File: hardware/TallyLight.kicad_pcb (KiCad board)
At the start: 4 copper layers, 68 x 68 mm, 136 parts, among them J1 Hanrun HY931147C, J2 USB_C_Receptacle_USB2.0, J3 Strapping, J4 UART, SW1 SW_Push, T2 HR051067, U1 ESP32-C3-MINI-1, U10 EL357N(B)(TA)-G, U11 CJ431, U2 KSZ8851SNL, U3 SRV05-4, U5 AMS1117-3.3, U7 SRV05-4, U9 Si3402-B, Y1 25MHz

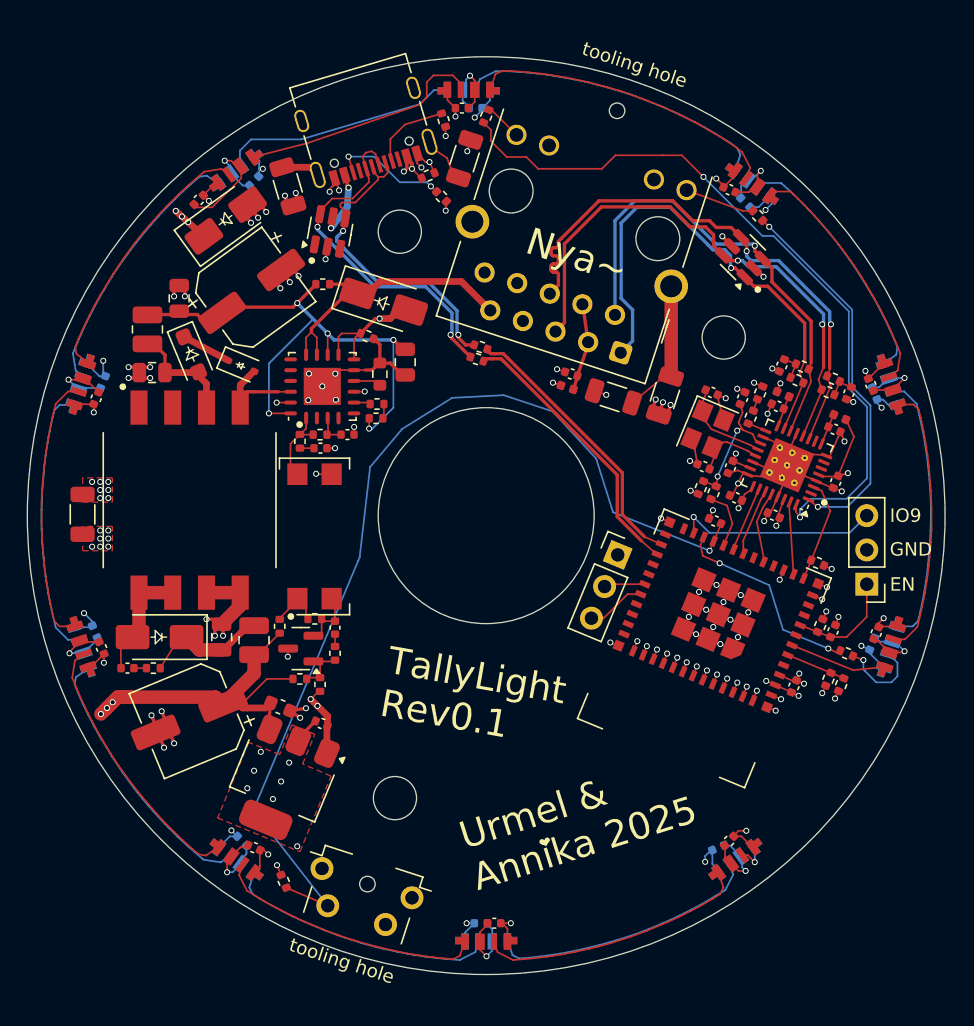
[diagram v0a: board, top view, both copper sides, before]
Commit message: hardware: replace ESP32-C3 MINI by more common WROOM-02 module
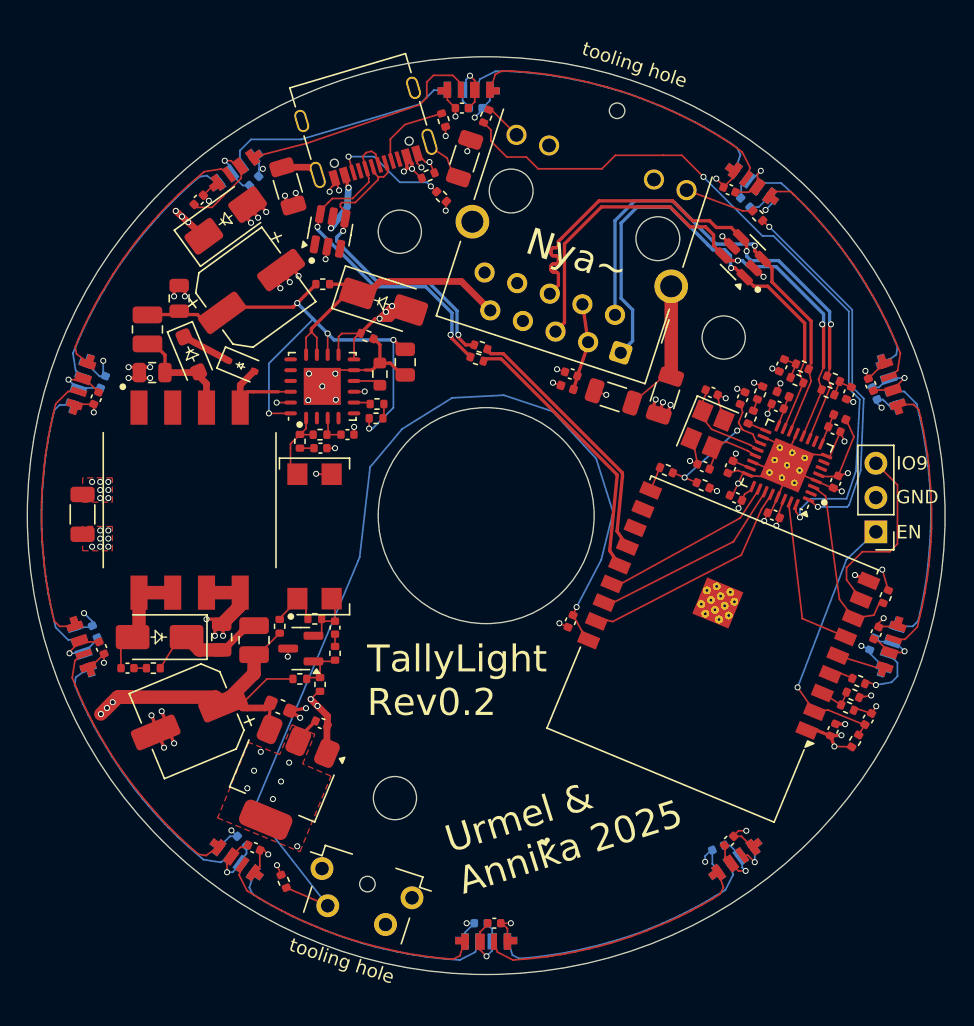
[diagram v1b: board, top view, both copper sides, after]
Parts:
- removed J4: UART, Connector_PinHeader_2.54mm:PinHeader_1x03_P2.54mm_Vertical
- removed U1: ESP32-C3-MINI-1, ESP32_C3:ESP32-C3-MINI-1
- added U4: ESP32-C3-WROOM-02, RF_Module:ESP32-C3-WROOM-02, F.Cu at (168.0, 107.0)
- moved C14 13.0 mm to (156.2, 107.8), turned to -112.5 degrees
- moved R2 8.93 mm to (177.3, 116.7), turned to 59.5 degrees
- moved C1 7.02 mm to (178.3, 115.1), turned to -120.5 degrees
- moved R4 5.63 mm to (179.6, 106.0), turned to 67.5 degrees
- moved C2 4.34 mm to (175.7, 115.9), turned to 67.5 degrees
- moved J3 3.94 mm to (178.9, 101.2)
- moved R3 3.88 mm to (163.3, 96.6), turned to 157.5 degrees
- moved R1 2.24 mm to (177.6, 112.3)
- moved R50 2.16 mm to (177.2, 113.3), turned to 157.5 degrees
- moved R49 1.77 mm to (176.8, 114.2), turned to -22.5 degrees
- moved R5 0.24 mm to (166.1, 97.8), turned to -22.5 degrees
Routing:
- net GND: track 182.8 -> 143.7 mm, vias 103 -> 70
- net /Logic/LED_Din: track 14.9 -> 1.11 mm, vias 2 -> 0
- net /Logic/EN: track 8.14 -> 20.2 mm, vias 0 -> 1
- net Net-(U2-SCLK): track 5.21 -> 16.5 mm
- net Net-(U2-SO): track 4.82 -> 14.3 mm
- net Net-(U2-~{CS}): track 4.69 -> 13.2 mm
- net Net-(U2-SI): track 5.10 -> 12.2 mm
- net Net-(U2-~{INT}): track 7.66 -> 13.2 mm
- net Net-(J4-Pin_3): track 4.48 -> 0.00 mm
- net /Logic/PoE-: track 18.3 -> 22.6 mm, vias 1 -> 3
- net /LEDs top/Din: track 7.27 -> 3.50 mm
- net Net-(J4-Pin_2): track 3.04 -> 0.00 mm
- net +3V3: track 13.5 -> 16.2 mm, vias 19 -> 18
- net Net-(U4-IO10): track 4.42 -> 1.86 mm
- net /LEDs bottom/Dout: track 6.48 -> 4.61 mm
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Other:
- board text added: "TallyLight Rev0.2"
- board text removed: "TallyLight Rev0.1"

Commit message: hardware: add testpoints to flyback converter and SPI MAC + Phy
Add testpoints to all critical section that might require in-circuit
debugging
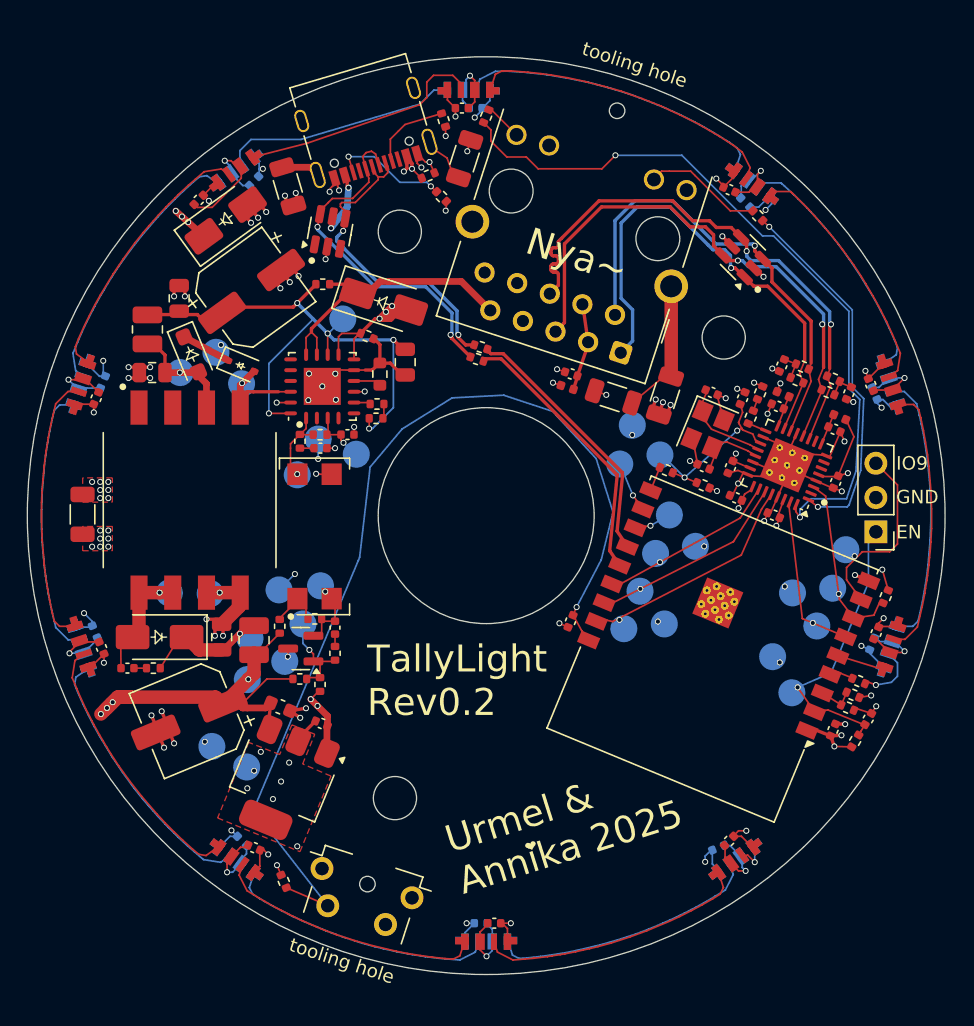
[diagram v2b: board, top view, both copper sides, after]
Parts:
- added TP1: EROUT, TestPoint_no_outline:TestPoint_Pad_D2.0mm_no_outline, B.Cu at (136.0, 97.0)
- added TP10: VOPTO, TestPoint_no_outline:TestPoint_Pad_D2.0mm_no_outline, B.Cu at (137.7, 105.2)
- added TP11: GND, TestPoint:TestPoint_Pad_D2.0mm, B.Cu at (134.7, 105.5)
- added TP12: VOUT, TestPoint_no_outline:TestPoint_Pad_D2.0mm_no_outline, B.Cu at (132.5, 109.1)
- added TP13: VOUT_FLYBACK, TestPoint_no_outline:TestPoint_Pad_D2.0mm_no_outline, B.Cu at (126.5, 105.7)
- added TP14: GND2, TestPoint_polygon_outline:TestPoint_Pad_D2.0mm_trianglular_outline, B.Cu at (130.0, 87.9)
- added TP15: RXD, TestPoint_no_outline:TestPoint_Pad_D2.0mm_no_outline, B.Cu at (159.9, 96.2)
- added TP16: TXD, TestPoint_no_outline:TestPoint_Pad_D2.0mm_no_outline, B.Cu at (163.6, 100.0)
- added TP17: SI, TestPoint_no_outline:TestPoint_Pad_D2.0mm_no_outline, B.Cu at (174.5, 108.2)
- added TP18: ~{INT}, TestPoint_no_outline:TestPoint_Pad_D2.0mm_no_outline, B.Cu at (175.7, 105.4)
- added TP19: ~{RST}, TestPoint_no_outline:TestPoint_Pad_D2.0mm_no_outline, B.Cu at (162.9, 95.5)
- added TP2: GND2, TestPoint_polygon_outline:TestPoint_Pad_D2.0mm_trianglular_outline, B.Cu at (137.6, 94.3)
- added TP20: SCLK, TestPoint_no_outline:TestPoint_Pad_D2.0mm_no_outline, B.Cu at (160.2, 108.4)
- added TP21: SO, TestPoint_no_outline:TestPoint_Pad_D2.0mm_no_outline, B.Cu at (161.4, 105.6)
- added TP22: ~{CS}, TestPoint_no_outline:TestPoint_Pad_D2.0mm_no_outline, B.Cu at (162.6, 102.8)
- added TP23: GND, TestPoint:TestPoint_Pad_D2.0mm, B.Cu at (129.6, 105.8)
- added TP24: EN, TestPoint_no_outline:TestPoint_Pad_D2.0mm_no_outline, B.Cu at (172.7, 113.1)
- added TP25: GND, TestPoint:TestPoint_Pad_D2.0mm, B.Cu at (171.2, 110.5)
- added TP26: IO9, TestPoint_no_outline:TestPoint_Pad_D2.0mm_no_outline, B.Cu at (176.7, 102.5)
- added TP27: GND, TestPoint:TestPoint_Pad_D2.0mm, B.Cu at (165.5, 102.3)
- added TP28: GND, TestPoint:TestPoint_Pad_D2.0mm, B.Cu at (163.2, 108.0)
- added TP29: GND, TestPoint:TestPoint_Pad_D2.0mm, B.Cu at (172.7, 105.7)
- added TP3: VOUT_FLT, TestPoint_no_outline:TestPoint_Pad_D2.0mm_no_outline, B.Cu at (132.3, 112.2)
- added TP30: GND, TestPoint:TestPoint_Pad_D2.0mm, B.Cu at (160.8, 93.3)
- added TP31: +3v3, TestPoint_no_outline:TestPoint_Pad_D2.0mm_no_outline, B.Cu at (132.2, 118.6)
- added TP32: GND, TestPoint:TestPoint_Pad_D2.0mm, B.Cu at (129.7, 117.1)
- added TP4: GND, TestPoint:TestPoint_Pad_D2.0mm, B.Cu at (135.1, 110.8)
- added TP5: VCC_FLYBACK, TestPoint_no_outline:TestPoint_Pad_D2.0mm_no_outline, B.Cu at (127.3, 89.4)
- added TP6: VCC_PoE, TestPoint_no_outline:TestPoint_Pad_D2.0mm_no_outline, B.Cu at (139.4, 85.4)
- added TP7: SW_FLYBACK, TestPoint_no_outline:TestPoint_Pad_D2.0mm_no_outline, B.Cu at (131.9, 90.2)
- added TP8: VCC_AUX, TestPoint_no_outline:TestPoint_Pad_D2.0mm_no_outline, B.Cu at (140.4, 95.5)
- added TP9: VREF, TestPoint_no_outline:TestPoint_Pad_D2.0mm_no_outline, B.Cu at (136.4, 108.0)
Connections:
- J1 pad 11: Net-(J1-Pad11) -> +3V3
- J1 pad 12: GND -> Net-(J1-Pad12)
- R36 pad 2: Net-(J1-Pad11) -> Net-(J1-Pad12)
- U4 pad 11: unconnected-(U4-IO20/RXD-Pad11) -> Net-(U4-IO20/RXD)
- U4 pad 12: unconnected-(U4-IO21/TXD-Pad12) -> Net-(U4-IO21/TXD)
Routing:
- net Net-(J1-Pad12): track 0.00 -> 8.83 mm
- net Net-(J1-Pad11): track 5.19 -> 0.00 mm
- net Net-(U4-IO20/RXD): track 0.00 -> 3.74 mm, vias 0 -> 1
- net Net-(U11-REF): track 3.99 -> 7.07 mm, vias 0 -> 1
- net Net-(U4-IO21/TXD): track 0.00 -> 2.74 mm, vias 0 -> 1
- net Net-(U2-~{RST}): track 11.3 -> 13.9 mm
- net Net-(U9-VDD): track 2.23 -> 4.21 mm, vias 0 -> 1
- net GND: track 143.7 -> 145.3 mm, vias 70 -> 78
- net Net-(U9-FB): track 43.0 -> 44.5 mm
- net GND2: track 12.7 -> 14.2 mm, vias 21 -> 23
- net /Logic/EN: track 20.2 -> 21.0 mm
- net /Logic/IO9: track 13.9 -> 14.0 mm, vias 0 -> 1
- net Net-(U2-SCLK): track 16.5 -> 16.7 mm, vias 0 -> 1
- net Net-(U2-SI): vias 0 -> 1
- net Net-(U2-~{CS}): vias 0 -> 1
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
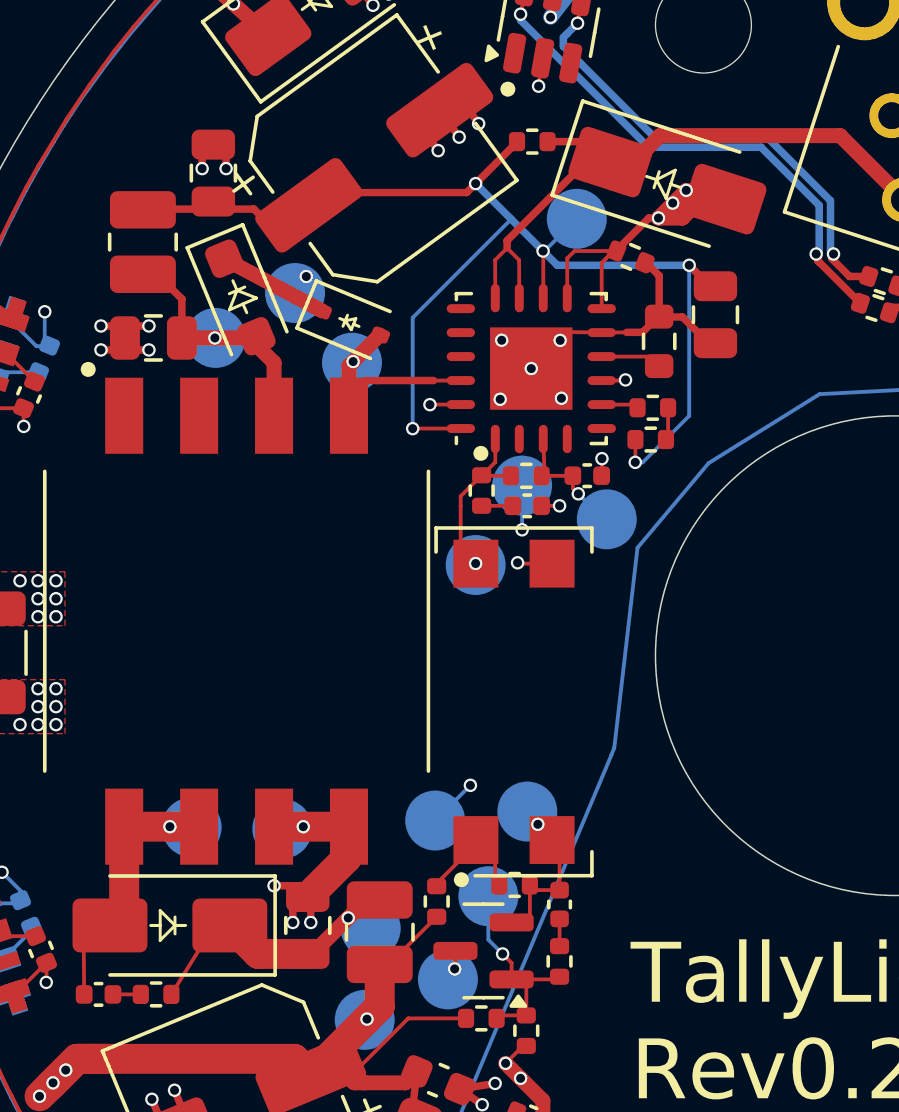
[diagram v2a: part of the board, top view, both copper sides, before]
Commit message: hardware: add small thermal plane to PoE controller
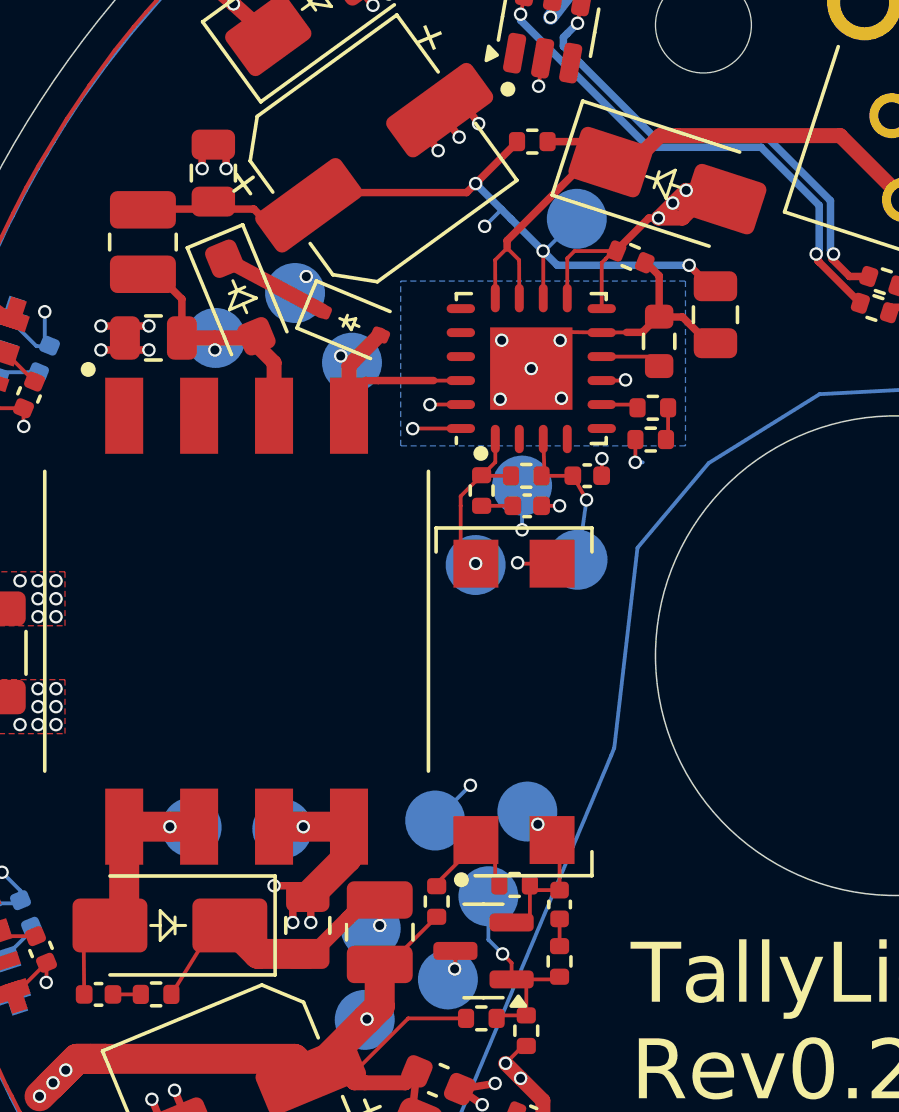
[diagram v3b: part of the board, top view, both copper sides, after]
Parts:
- moved TP8 1.67 mm to (139.4, 96.8)
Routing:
- net Net-(D28-K): track 11.7 -> 12.6 mm
- net Net-(U9-FB): track 44.5 -> 44.8 mm, vias 5 -> 6
- added copper zone on B.Cu, net Net-(C49-Pad2)
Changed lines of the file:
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@@
 	(footprint "TestPoint_no_outline:TestPoint_Pad_D2.0mm_no_outline"
 		(layer "B.Cu")
-		(at 140.375 95.45 180)
+		(at 139.4 96.8 180)
 		(descr "SMD pad as test Point, diameter 2.0mm")
 		(tags "test point SMD pad")
@@
 		(net 3)
 	)
+	(segment
+		(start 127.3 89.4)
+		(end 127.3 89.8)
+		(width 0.127)
+		(layer "F.Cu")
+		(net 3)
+	)
 	(via
-		(at 127.3 89.4)
+		(at 127.3 89.8)
 		(size 0.45)
 		(drill 0.3)
@@
 	)
 	(segment
-		(start 139.242677 94.417677)
-		(end 139.425 94.6)
+		(start 138.2 94)
+		(end 139.2 94)
 		(width 0.127)
 		(layer "F.Cu")
@@
 	(segment
 		(start 139.242677 93.995228)
-		(end 139.242677 94.417677)
-		(width 0.127)
-		(layer "F.Cu")
-		(net 5)
-	)
-	(segment
-		(start 138.2 94)
-		(end 139.2 94)
+		(end 139.699334 94.800665)
 		(width 0.127)
 		(layer "F.Cu")
@@
 	)
 	(via
-		(at 139.425 94.6)
+		(at 139.699334 94.800665)
 		(size 0.45)
 		(drill 0.3)
@@
 	)
 	(segment
-		(start 140.325 95.5)
-		(end 140.35 95.5)
-		(width 0.127)
-		(layer "B.Cu")
-		(net 5)
-	)
-	(segment
-		(start 139.425 94.6)
-		(end 140.325 95.5)
+		(start 139.699334 94.800665)
+		(end 139.5 96.2)
 		(width 0.127)
 		(layer "B.Cu")
@@
 	)
 	(segment
+		(start 132.8 108.150002)
+		(end 132.8 109)
+		(width 0.127)
+		(layer "F.Cu")
+		(net 17)
+	)
+	(segment
 		(start 132.349998 108.150002)
 		(end 131.9 108.6)
@@
 	)
 	(via
-		(at 131.75 108.75)
+		(at 132.8 109)
 		(size 0.45)
 		(drill 0.3)
@@
 	)
 	(segment
+		(start 131.775003 90.324997)
+		(end 131.5 90)
+		(width 0.127)
+		(layer "F.Cu")
+		(net 38)
+	)
+	(segment
 		(start 134.6 90.821081)
 		(end 132.75 90.821081)
@@
 	)
 	(via
-		(at 131.9125 90.1875)
+		(at 131.5 90)
 		(size 0.45)
 		(drill 0.3)
@@
 	)
 	(via
+		(at 136.3 85.675)
+		(size 0.45)
+		(drill 0.3)
+		(layers "F.Cu" "B.Cu")
+		(net 81)
+	)
+	(via
 		(at 143.125 86.975)
 		(size 0.45)
@@
 	)
 	(segment
-		(start 137.1875 85.4375)
-		(end 136 84.25)
-		(width 0.25)
-		(layer "B.Cu")
+		(start 133.9 88.075)
+		(end 136.3 85.675)
+		(width 0.127)
+		(layer "In2.Cu")
 		(net 81)
 	)
 	(segment
-		(start 133.9 92.425)
-		(end 133.9 88.725)
+		(start 143.125 91.75)
+		(end 143.125 86.975)
 		(width 0.127)
-		(layer "B.Cu")
+		(layer "In2.Cu")
 		(net 81)
 	)
 	(segment
-		(start 138.725 86.975)
-		(end 138.25 86.5)
-		(width 0.25)
-		(layer "B.Cu")
+		(start 133.9 92.425)
+		(end 133.9 88.075)
+		(width 0.127)
+		(layer "In2.Cu")
 		(net 81)
 	)
 	(segment
-		(start 141.575 93.55)
-		(end 143.125 92)
+		(start 141.325 93.55)
+		(end 143.125 91.75)
 		(width 0.127)
+		(layer "In2.Cu")
+		(net 81)
+	)
+	(segment
+		(start 136.8625 85.1125)
+		(end 136 84.25)
+		(width 0.25)
 		(layer "B.Cu")
 		(net 81)
 	)
 	(segment
-		(start 133.9 88.725)
-		(end 137.1875 85.4375)
-		(width 0.127)
+		(start 138.725 86.975)
+		(end 138.25 86.5)
+		(width 0.25)
 		(layer "B.Cu")
 		(net 81)
@@
 	)
 	(segment
-		(start 143.125 92)
-		(end 143.125 86.975)
+		(start 137.1875 85.4375)
+		(end 136.8625 85.1125)
+		(width 0.25)
+		(layer "B.Cu")
+		(net 81)
+	)
+	(segment
+		(start 136.3 85.675)
+		(end 136.8625 85.1125)
 		(width 0.127)
 		(layer "B.Cu")
@@
 			(pts
 				(xy 126.7 81.8) (xy 135.5 79.4) (xy 136.9 81.4) (xy 146 84.1) (xy 145.2 90.2) (xy 143 93.3) (xy 140.3 95.4)
-				(xy 140 100) (xy 120.3 100) (xy 120.5 96.6) (xy 121.2 93.4) (xy 122 90.3) (xy 123.2 87.4) (xy 124.4 85.1)
+				(xy 140 100) (xy 120.5 100) (xy 120.5 96.6) (xy 121.2 93.4) (xy 122 90.3) (xy 123.2 87.4) (xy 124.4 85.1)
 				(xy 125.7 83.2)
 			)
@@
 			)
 		)
+	)
+	(zone
+		(net 79)
+		(net_name "Net-(C49-Pad2)")
+		(layer "B.Cu")
+		(hatch edge 0.5)
+		(priority 2)
+		(connect_pads yes
+			(clearance 0.25)
+		)
+		(min_thickness 0.25)
+		(filled_areas_thickness no)
+		(fill yes
+			(thermal_gap 0.5)
+			(thermal_bridge_width 0.5)
+		)
+		(polygon
+			(pts
+				(xy 143 93) (xy 133.5 93) (xy 133.5 87.5) (xy 143 87.5)
+			)
+		)
